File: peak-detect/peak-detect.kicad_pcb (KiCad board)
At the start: 4 copper layers, 33 x 59.7 mm, 73 parts, among them J1 CONN_02X05, J2 CONN_01X03, J3 CONN_01X03, J4 CONN_01X03, J5 CONN_01X03, Q1 BC847, Q2 BC847, U1 LM358, U2 LM358, U3 OPA2134

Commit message: Updated to Kicad 5
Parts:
- removed REF** (x3): MountingHole_2.2mm_M2_DIN965, Mounting_Holes:MountingHole_2.2mm_M2_DIN965
- J1: value CONN_02X05 -> Conn_02x05_Odd_Even
- U3: value OPA2134 -> LM358
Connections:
- RL1 pad 2: (no net) -> Net-(RL1-Pad2)
- RL1 pad 7: (no net) -> Net-(RL1-Pad7)
- RL2 pad 2: (no net) -> Net-(RL2-Pad2)
- RL2 pad 7: (no net) -> Net-(RL2-Pad7)

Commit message: Combine libraries
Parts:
- RL1, RL2: footprint lci-relays:Omron-G6K -> lci-kicad:Omron-G6K
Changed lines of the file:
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@@
     (add_net U1-)
+  )
+  (module lci-kicad:Omron-G6K (layer F.Cu)
+    (at 171.704 89.916)
+    (fp_text reference RL2 (at 0 0) (layer F.Fab)
+      (effects (font (size 1.5 1.5) (thickness 0.15)))
+    )
+    (fp_text value Omron_G6K (at -7.62 0 90) (layer F.SilkS) hide
+      (effects (font (size 1.5 1.5) (thickness 0.15)))
+    )
+    (fp_line (start -5.588 3.175) (end -5.588 2.286) (layer F.SilkS) (width 0.15))
+    (fp_line (start -5.08 3.175) (end -5.588 3.175) (layer F.SilkS) (width 0.15))
+    (fp_line (start -5.08 2.286) (end -5.08 3.175) (layer F.SilkS) (width 0.15))
+    (fp_line (start -5.588 2.286) (end -5.08 2.286) (layer F.SilkS) (width 0.15))
+    (fp_line (start -6.35 3.81) (end -6.35 -3.81) (layer F.SilkS) (width 0.15))
+    (fp_line (start 6.35 3.81) (end -6.35 3.81) (layer F.SilkS) (width 0.15))
+    (fp_line (start 6.35 -3.81) (end 6.35 3.81) (layer F.SilkS) (width 0.15))
+    (fp_line (start -6.35 -3.81) (end 6.35 -3.81) (layer F.SilkS) (width 0.15))
+    (pad 5 thru_hole circle (at 3.81 -2.54) (size 1.524 1.524) (drill 0.762) (layers *.Cu *.Mask F.SilkS)
+      (net 13 Out-Right))
+    (pad 6 thru_hole circle (at 1.27 -2.54) (size 1.524 1.524) (drill 0.762) (layers *.Cu *.Mask F.SilkS)
+      (net 18 In-Right-2))
+    (pad 7 thru_hole circle (at -1.27 -2.54) (size 1.524 1.524) (drill 0.762) (layers *.Cu *.Mask F.SilkS)
+      (net 47 "Net-(RL2-Pad7)"))
+    (pad 8 thru_hole circle (at -3.81 -2.54) (size 1.524 1.524) (drill 0.762) (layers *.Cu *.Mask F.SilkS)
+      (net 37 "Net-(D4-2-Pad2)"))
+    (pad 4 thru_hole circle (at 3.81 2.54) (size 1.524 1.524) (drill 0.762) (layers *.Cu *.Mask F.SilkS)
+      (net 14 Out-Left))
+    (pad 3 thru_hole circle (at 1.27 2.54) (size 1.524 1.524) (drill 0.762) (layers *.Cu *.Mask F.SilkS)
+      (net 17 In-Left-2))
+    (pad 2 thru_hole circle (at -1.27 2.54) (size 1.524 1.524) (drill 0.762) (layers *.Cu *.Mask F.SilkS)
+      (net 46 "Net-(RL2-Pad2)"))
+    (pad 1 thru_hole rect (at -3.81 2.54) (size 1.524 1.524) (drill 0.762) (layers *.Cu *.Mask F.SilkS)
+      (net 4 +5V))
+  )
+  (module lci-kicad:Omron-G6K (layer F.Cu)
+    (at 171.704 68.58)
+    (fp_text reference RL1 (at 0 0) (layer F.Fab)
+      (effects (font (size 1.5 1.5) (thickness 0.15)))
+    )
+    (fp_text value Omron_G6K (at -7.62 0 90) (layer F.SilkS) hide
+      (effects (font (size 1.5 1.5) (thickness 0.15)))
+    )
+    (fp_line (start -6.35 -3.81) (end 6.35 -3.81) (layer F.SilkS) (width 0.15))
+    (fp_line (start 6.35 -3.81) (end 6.35 3.81) (layer F.SilkS) (width 0.15))
+    (fp_line (start 6.35 3.81) (end -6.35 3.81) (layer F.SilkS) (width 0.15))
+    (fp_line (start -6.35 3.81) (end -6.35 -3.81) (layer F.SilkS) (width 0.15))
+    (fp_line (start -5.588 2.286) (end -5.08 2.286) (layer F.SilkS) (width 0.15))
+    (fp_line (start -5.08 2.286) (end -5.08 3.175) (layer F.SilkS) (width 0.15))
+    (fp_line (start -5.08 3.175) (end -5.588 3.175) (layer F.SilkS) (width 0.15))
+    (fp_line (start -5.588 3.175) (end -5.588 2.286) (layer F.SilkS) (width 0.15))
+    (pad 1 thru_hole rect (at -3.81 2.54) (size 1.524 1.524) (drill 0.762) (layers *.Cu *.Mask F.SilkS)
+      (net 4 +5V))
+    (pad 2 thru_hole circle (at -1.27 2.54) (size 1.524 1.524) (drill 0.762) (layers *.Cu *.Mask F.SilkS)
+      (net 44 "Net-(RL1-Pad2)"))
+    (pad 3 thru_hole circle (at 1.27 2.54) (size 1.524 1.524) (drill 0.762) (layers *.Cu *.Mask F.SilkS)
+      (net 15 In-Left-1))
+    (pad 4 thru_hole circle (at 3.81 2.54) (size 1.524 1.524) (drill 0.762) (layers *.Cu *.Mask F.SilkS)
+      (net 14 Out-Left))
+    (pad 8 thru_hole circle (at -3.81 -2.54) (size 1.524 1.524) (drill 0.762) (layers *.Cu *.Mask F.SilkS)
+      (net 36 "Net-(D4-1-Pad2)"))
+    (pad 7 thru_hole circle (at -1.27 -2.54) (size 1.524 1.524) (drill 0.762) (layers *.Cu *.Mask F.SilkS)
+      (net 45 "Net-(RL1-Pad7)"))
+    (pad 6 thru_hole circle (at 1.27 -2.54) (size 1.524 1.524) (drill 0.762) (layers *.Cu *.Mask F.SilkS)
+      (net 16 In-Right-1))
+    (pad 5 thru_hole circle (at 3.81 -2.54) (size 1.524 1.524) (drill 0.762) (layers *.Cu *.Mask F.SilkS)
+      (net 13 Out-Right))
   )
   (module Resistors_SMD:R_0603_HandSoldering (layer F.Cu)
@@
     )
   )
-  (module lci-relays:Omron-G6K (layer F.Cu)
-    (at 171.704 68.58)
-    (fp_text reference RL1 (at 0 0) (layer F.Fab)
-      (effects (font (size 1.5 1.5) (thickness 0.15)))
-    )
-    (fp_text value Omron_G6K (at -7.62 0 90) (layer F.SilkS) hide
-      (effects (font (size 1.5 1.5) (thickness 0.15)))
-    )
-    (fp_line (start -6.35 -3.81) (end 6.35 -3.81) (layer F.SilkS) (width 0.15))
-    (fp_line (start 6.35 -3.81) (end 6.35 3.81) (layer F.SilkS) (width 0.15))
-    (fp_line (start 6.35 3.81) (end -6.35 3.81) (layer F.SilkS) (width 0.15))
-    (fp_line (start -6.35 3.81) (end -6.35 -3.81) (layer F.SilkS) (width 0.15))
-    (fp_line (start -5.588 2.286) (end -5.08 2.286) (layer F.SilkS) (width 0.15))
-    (fp_line (start -5.08 2.286) (end -5.08 3.175) (layer F.SilkS) (width 0.15))
-    (fp_line (start -5.08 3.175) (end -5.588 3.175) (layer F.SilkS) (width 0.15))
-    (fp_line (start -5.588 3.175) (end -5.588 2.286) (layer F.SilkS) (width 0.15))
-    (pad 1 thru_hole rect (at -3.81 2.54) (size 1.524 1.524) (drill 0.762) (layers *.Cu *.Mask F.SilkS)
-      (net 4 +5V))
-    (pad 2 thru_hole circle (at -1.27 2.54) (size 1.524 1.524) (drill 0.762) (layers *.Cu *.Mask F.SilkS)
-      (net 44 "Net-(RL1-Pad2)"))
-    (pad 3 thru_hole circle (at 1.27 2.54) (size 1.524 1.524) (drill 0.762) (layers *.Cu *.Mask F.SilkS)
-      (net 15 In-Left-1))
-    (pad 4 thru_hole circle (at 3.81 2.54) (size 1.524 1.524) (drill 0.762) (layers *.Cu *.Mask F.SilkS)
-      (net 14 Out-Left))
-    (pad 8 thru_hole circle (at -3.81 -2.54) (size 1.524 1.524) (drill 0.762) (layers *.Cu *.Mask F.SilkS)
-      (net 36 "Net-(D4-1-Pad2)"))
-    (pad 7 thru_hole circle (at -1.27 -2.54) (size 1.524 1.524) (drill 0.762) (layers *.Cu *.Mask F.SilkS)
-      (net 45 "Net-(RL1-Pad7)"))
-    (pad 6 thru_hole circle (at 1.27 -2.54) (size 1.524 1.524) (drill 0.762) (layers *.Cu *.Mask F.SilkS)
-      (net 16 In-Right-1))
-    (pad 5 thru_hole circle (at 3.81 -2.54) (size 1.524 1.524) (drill 0.762) (layers *.Cu *.Mask F.SilkS)
-      (net 13 Out-Right))
-  )
-  (module lci-relays:Omron-G6K (layer F.Cu)
-    (at 171.704 89.916)
-    (fp_text reference RL2 (at 0 0) (layer F.Fab)
-      (effects (font (size 1.5 1.5) (thickness 0.15)))
-    )
-    (fp_text value Omron_G6K (at -7.62 0 90) (layer F.SilkS) hide
-      (effects (font (size 1.5 1.5) (thickness 0.15)))
-    )
-    (fp_line (start -6.35 -3.81) (end 6.35 -3.81) (layer F.SilkS) (width 0.15))
-    (fp_line (start 6.35 -3.81) (end 6.35 3.81) (layer F.SilkS) (width 0.15))
-    (fp_line (start 6.35 3.81) (end -6.35 3.81) (layer F.SilkS) (width 0.15))
-    (fp_line (start -6.35 3.81) (end -6.35 -3.81) (layer F.SilkS) (width 0.15))
-    (fp_line (start -5.588 2.286) (end -5.08 2.286) (layer F.SilkS) (width 0.15))
-    (fp_line (start -5.08 2.286) (end -5.08 3.175) (layer F.SilkS) (width 0.15))
-    (fp_line (start -5.08 3.175) (end -5.588 3.175) (layer F.SilkS) (width 0.15))
-    (fp_line (start -5.588 3.175) (end -5.588 2.286) (layer F.SilkS) (width 0.15))
-    (pad 1 thru_hole rect (at -3.81 2.54) (size 1.524 1.524) (drill 0.762) (layers *.Cu *.Mask F.SilkS)
-      (net 4 +5V))
-    (pad 2 thru_hole circle (at -1.27 2.54) (size 1.524 1.524) (drill 0.762) (layers *.Cu *.Mask F.SilkS)
-      (net 46 "Net-(RL2-Pad2)"))
-    (pad 3 thru_hole circle (at 1.27 2.54) (size 1.524 1.524) (drill 0.762) (layers *.Cu *.Mask F.SilkS)
-      (net 17 In-Left-2))
-    (pad 4 thru_hole circle (at 3.81 2.54) (size 1.524 1.524) (drill 0.762) (layers *.Cu *.Mask F.SilkS)
-      (net 14 Out-Left))
-    (pad 8 thru_hole circle (at -3.81 -2.54) (size 1.524 1.524) (drill 0.762) (layers *.Cu *.Mask F.SilkS)
-      (net 37 "Net-(D4-2-Pad2)"))
-    (pad 7 thru_hole circle (at -1.27 -2.54) (size 1.524 1.524) (drill 0.762) (layers *.Cu *.Mask F.SilkS)
-      (net 47 "Net-(RL2-Pad7)"))
-    (pad 6 thru_hole circle (at 1.27 -2.54) (size 1.524 1.524) (drill 0.762) (layers *.Cu *.Mask F.SilkS)
-      (net 18 In-Right-2))
-    (pad 5 thru_hole circle (at 3.81 -2.54) (size 1.524 1.524) (drill 0.762) (layers *.Cu *.Mask F.SilkS)
-      (net 13 Out-Right))
-  )
   (module Diodes_SMD:D_0603 (layer B.Cu)

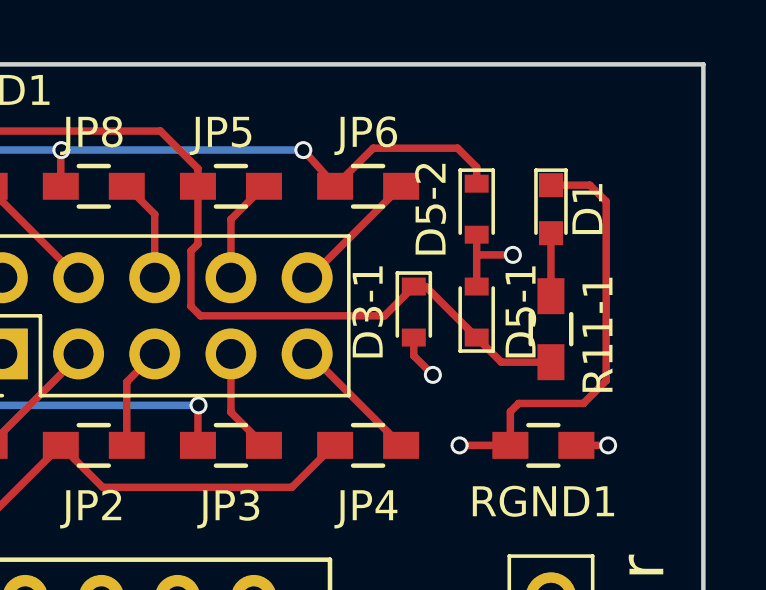
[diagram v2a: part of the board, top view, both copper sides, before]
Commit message: SOD-123 footprint for Zener diodes
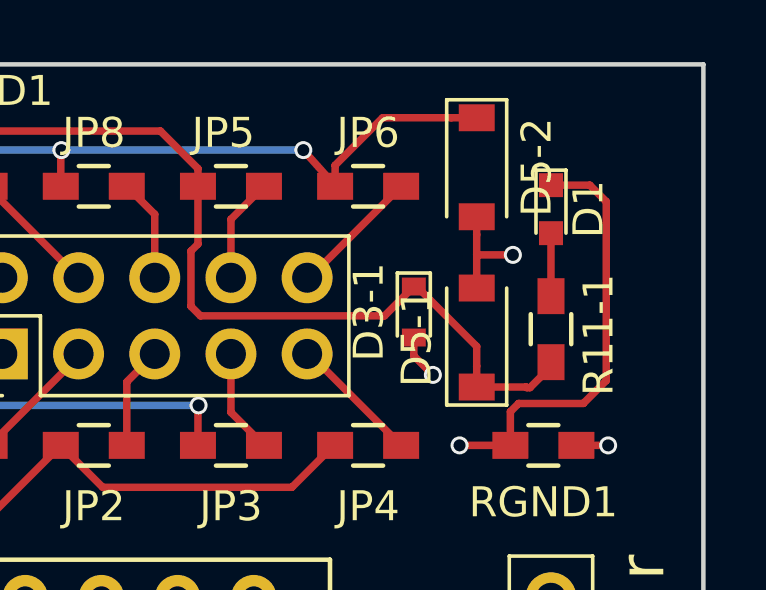
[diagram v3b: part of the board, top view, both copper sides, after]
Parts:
- D5-1, D5-2: value 5v -> 3.3V; footprint Diodes_SMD:D_0603 -> Diodes_SMD:D_SOD-123
- U1, U2, U3: value LM358 -> OP2134
- moved D5-2 1.40 mm to (182.9, 51.7)
- moved D5-1 0.85 mm to (182.9, 57.4)
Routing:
- net Out-Peak-1: track 66.6 -> 68.2 mm
- net GNDD: track 57.6 -> 58.2 mm

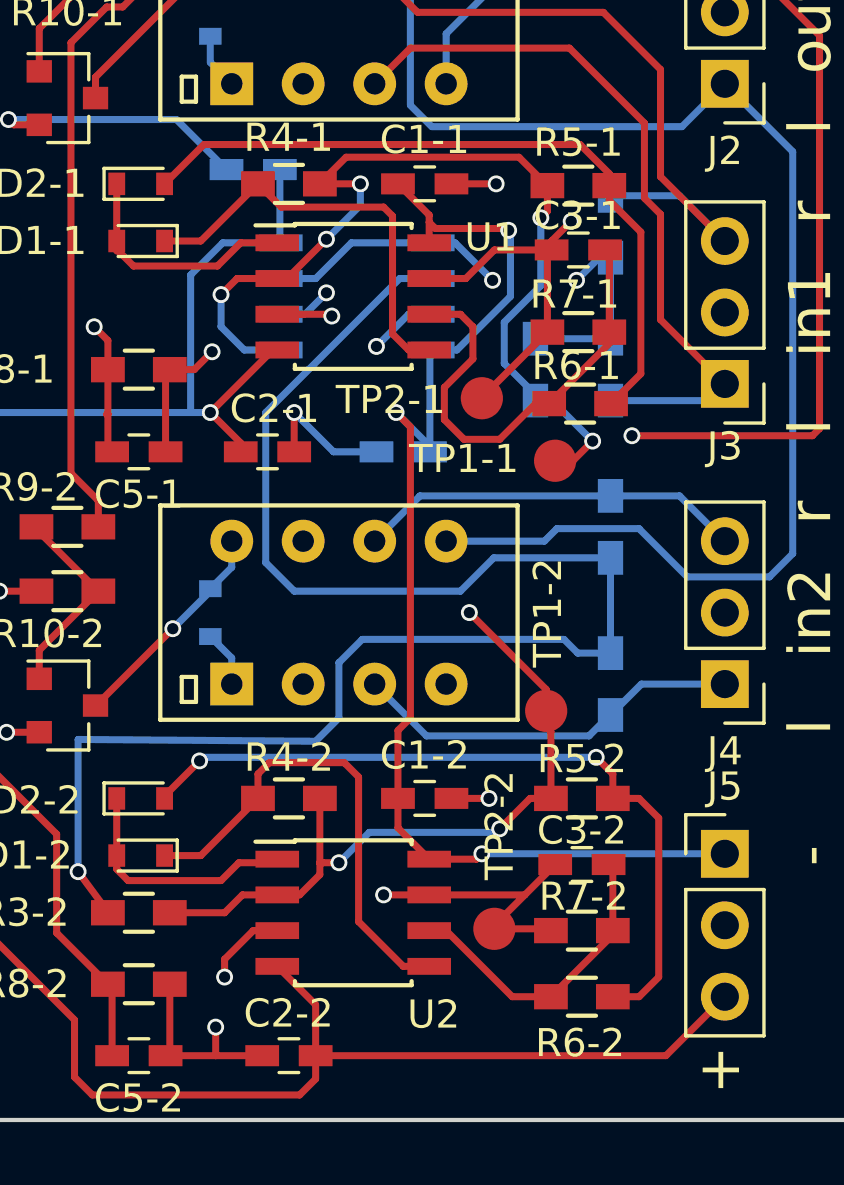
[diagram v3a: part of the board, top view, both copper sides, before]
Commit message: Fix footprints
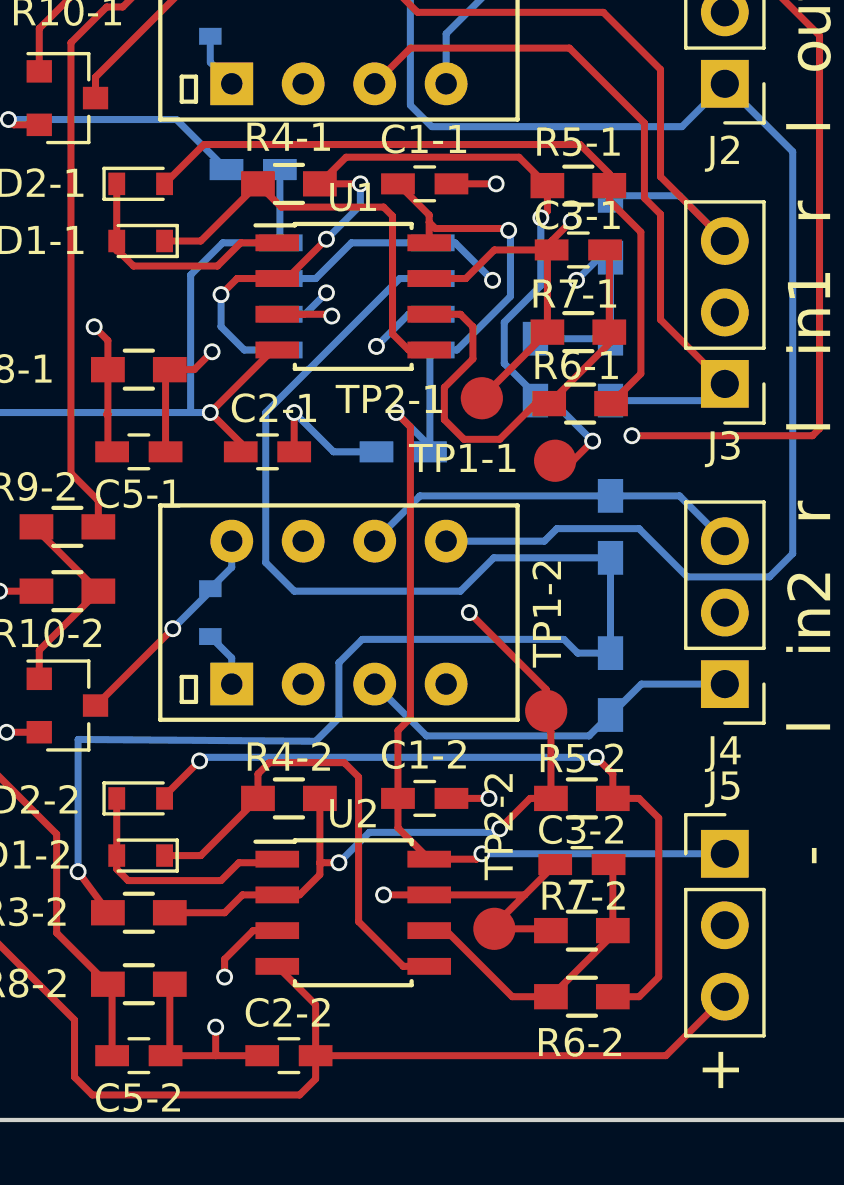
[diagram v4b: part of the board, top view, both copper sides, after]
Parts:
- U1, U2, U3: value OP2134 -> OPA2134; footprint Housings_SOIC:SOIC-8_3.9x4.9mm_Pitch1.27mm -> Package_SO:SOIC-8_3.9x4.9mm_P1.27mm
